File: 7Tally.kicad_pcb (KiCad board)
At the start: 2 copper layers, 53 x 35 mm, 49 parts, among them J2 B2B-PH-K-S_LF__SN_, P1 53047-0310, SW1 TL3300CF160Q, U1 ESP32-C3_SUPERMINI_TH, U2 BQ21040DBVR, U3 TC1263-3.3VOA

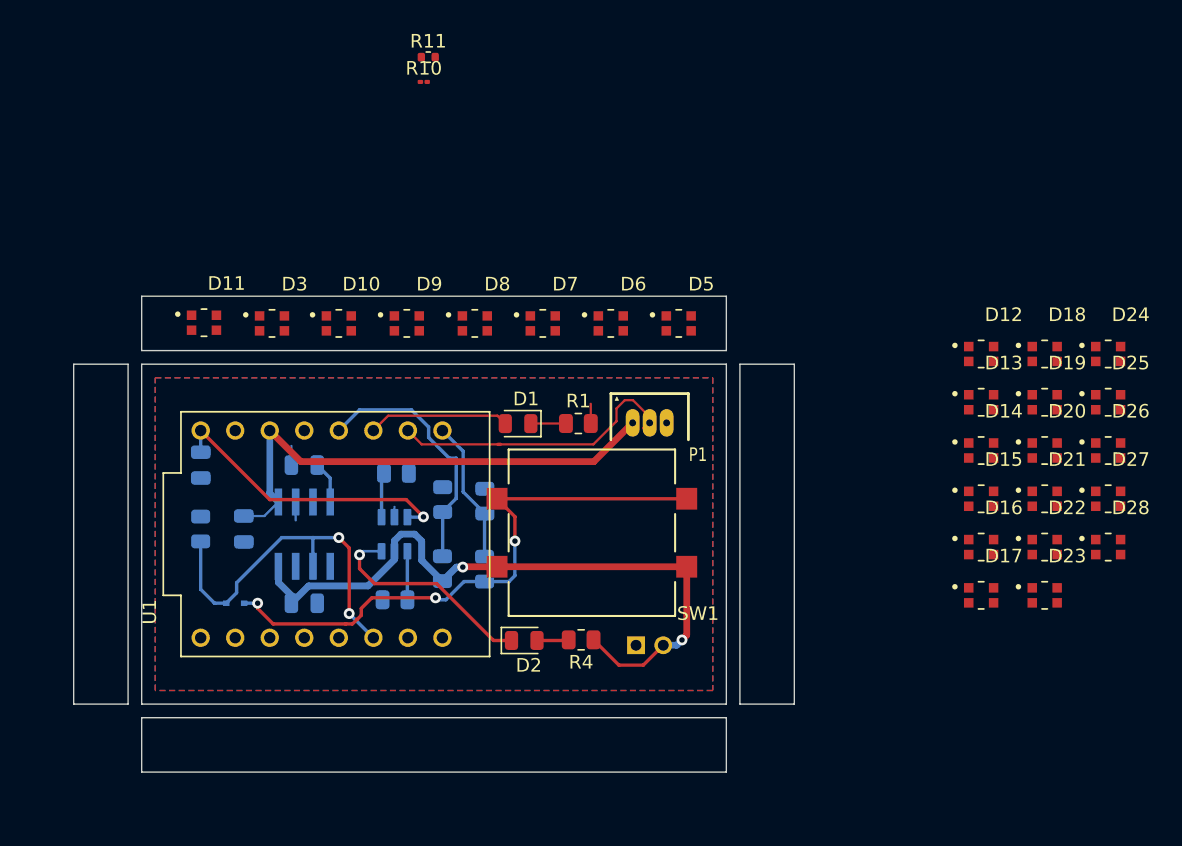
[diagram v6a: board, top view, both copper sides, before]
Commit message: feat(PCB): start of castellated edges implementation
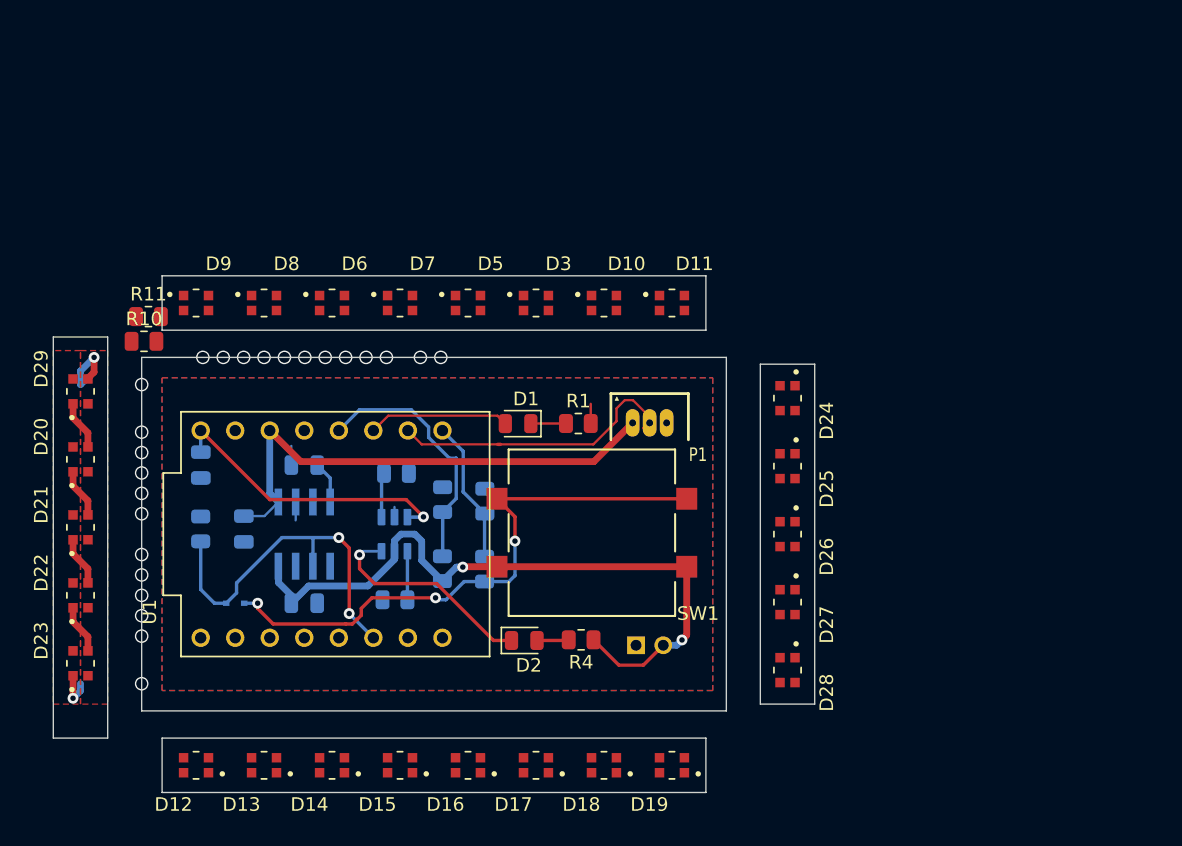
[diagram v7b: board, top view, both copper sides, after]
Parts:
- added D29: WS2812B2020, WS2812B2020:LED_WS2812B2020, F.Cu at (44.5, 53.0)
- R10: footprint Resistor_SMD:R_01005_0402Metric -> Resistor_SMD:R_0805_2012Metric
- R11: footprint Resistor_SMD:R_0402_1005Metric -> Resistor_SMD:R_0805_2012Metric
- moved D23 71.1 mm to (44.5, 73.0), turned to 90 degrees
- moved D22 71.0 mm to (44.5, 68.0), turned to 90 degrees
- moved D21 70.9 mm to (44.5, 63.0), turned to 90 degrees
- moved D20 70.9 mm to (44.5, 58.0), turned to 90 degrees
- moved D12 65.2 mm to (53.0, 80.5), turned to 180 degrees
- moved D13 59.1 mm to (58.0, 80.5), turned to 180 degrees
- moved D14 53.1 mm to (63.0, 80.5), turned to 180 degrees
- moved D15 47.0 mm to (68.0, 80.5), turned to 180 degrees
- moved D18 44.3 mm to (83.0, 80.5), turned to 180 degrees
- moved D16 41.0 mm to (73.0, 80.5), turned to 180 degrees
- moved D19 38.3 mm to (88.0, 80.5), turned to 180 degrees
- moved D17 35.0 mm to (78.0, 80.5), turned to 180 degrees
- moved D11 34.4 mm to (88.0, 46.5)
- moved R10 28.1 mm to (49.2, 49.3)
- moved R11 28.1 mm to (49.5, 47.5)
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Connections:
- D11 pad 3: unconnected-(D11-DI-Pad3) -> Net-(D11-DI)
- D12 pad 3: unconnected-(D12-DI-Pad3) -> Net-(D12-DI)
- D19 pad 1: unconnected-(D19-DO-Pad1) -> Net-(D11-DI)
- D20 pad 3: unconnected-(D20-DI-Pad3) -> Net-(D20-DI)
- D23 pad 1: unconnected-(D23-DO-Pad1) -> Net-(D23-DO)
- D24 pad 3: unconnected-(D24-DI-Pad3) -> Net-(D23-DO)
- D28 pad 1: unconnected-(D28-DO-Pad1) -> Net-(D12-DI)
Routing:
- net NEOPIXEL_PIN: track 22.0 -> 26.9 mm, vias 0 -> 1
- net Net-(D20-DO): track 0.00 -> 3.63 mm
- net Net-(D20-DI): track 0.00 -> 3.63 mm
- net Net-(D21-DO): track 0.00 -> 3.63 mm
- net Net-(D22-DO): track 0.00 -> 3.63 mm
- net Net-(D23-DO): track 0.00 -> 3.06 mm, vias 0 -> 1
- net VBAT: vias 2 -> 3
- net Led_Vdd: vias 0 -> 6
- net GND: vias 0 -> 5
- net (no net): vias 0 -> 12
- added copper zone on F.Cu, net Led_Vdd
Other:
- board size 53 x 35 mm -> 56 x 38 mm

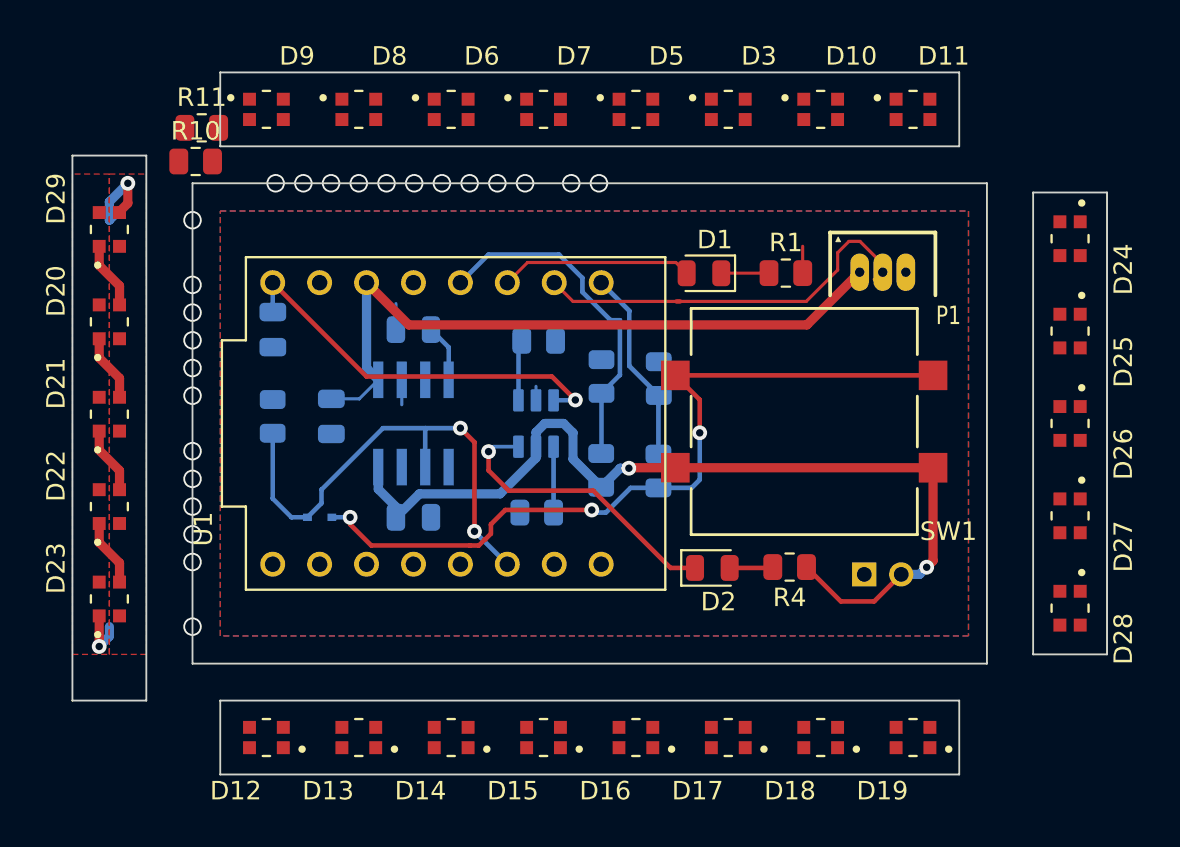
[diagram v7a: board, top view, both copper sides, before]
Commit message: feat(PCB): finalized initial PCB
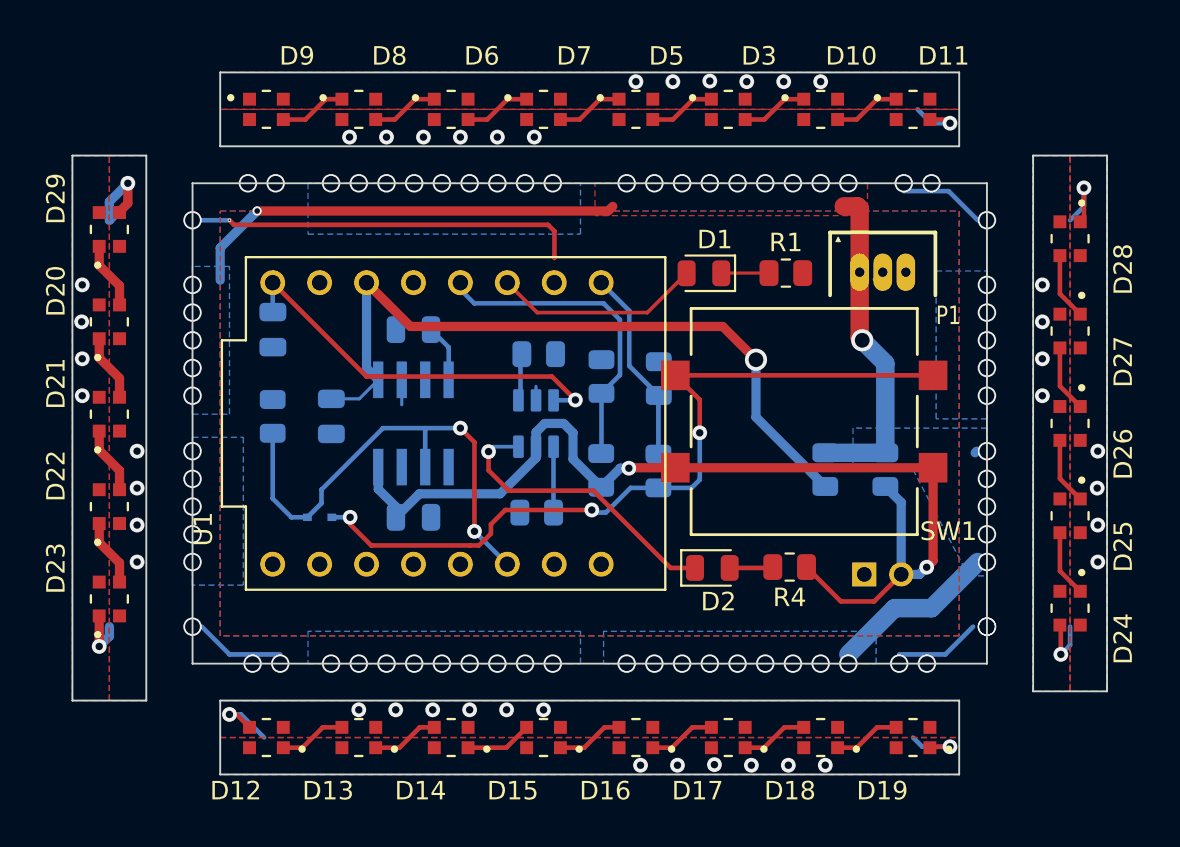
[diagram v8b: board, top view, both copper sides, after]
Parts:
- R10, R11: moved to B.Cu
- moved R11 41.4 mm to (86.5, 66.0), turned to 90 degrees
- moved R10 37.9 mm to (83.2, 66.0), turned to 90 degrees
- moved D24 20.0 mm to (96.5, 73.5)
- moved D28 20.0 mm to (96.5, 53.5)
- moved D25 10.0 mm to (96.5, 68.5)
- moved D27 10.0 mm to (96.5, 58.5)
- moved R2 0.72 mm to (67.7, 59.8)
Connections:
- D19 pad 1: Net-(D11-DI) -> Net-(D19-DO)
- D23 pad 1: Net-(D23-DO) -> Net-(D12-DI)
- D24 pad 3: Net-(D23-DO) -> Net-(D19-DO)
- D28 pad 1: Net-(D12-DI) -> Net-(D11-DI)
- P1 pad 1: +3.3V -> Led_Vdd
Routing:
- net Led_Vdd: track 0.00 -> 51.3 mm, vias 6 -> 50
- net Net-(D11-DI): track 0.00 -> 11.9 mm, vias 0 -> 5
- net Net-(D12-DI): track 0.00 -> 11.7 mm, vias 0 -> 5
- net Net-(D19-DO): track 0.00 -> 11.2 mm, vias 0 -> 6
- net VBAT: track 51.4 -> 56.5 mm, vias 3 -> 2
- net Net-(D6-DO): track 0.00 -> 3.63 mm
- net Net-(D13-DO): track 0.00 -> 3.63 mm
- net Net-(D12-DO): track 0.00 -> 3.63 mm
- net Net-(D8-DO): track 0.00 -> 3.63 mm
- net Net-(D27-DO): track 0.00 -> 3.63 mm
- net Net-(D26-DO): track 0.00 -> 3.63 mm
- net Net-(D6-DI): track 0.00 -> 3.63 mm
- net Net-(D14-DO): track 0.00 -> 3.63 mm
- net Net-(D5-DO): track 0.00 -> 3.63 mm
- net Net-(D3-DO): track 0.00 -> 3.63 mm
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- added copper zone on B.Cu, net Led_Vdd
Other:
- outline, holes or cut-outs redrawn
